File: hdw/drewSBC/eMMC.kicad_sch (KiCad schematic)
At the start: 0 parts

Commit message: added emmc sheet contents
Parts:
- added C? (x4): 0.1uF, Capacitors_SMD:C_0402, symbol Custom_Library:C_Custom
- added C?: 2.2uF, Capacitors_SMD:C_0402, symbol Custom_Library:C_Custom
- added C?: 10uF, Capacitors_SMD:C_1206, symbol Custom_Library:C_Custom
- added R? (x11): 10k, Resistors_SMD:R_0402, symbol Custom_Library:R_Custom
- added U?: EMMC04G-M627-A01, BGA153C50P14X14_1300X1150X100, symbol Custom Library:EMMC04G-M627-A01
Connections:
- new net: C?.1, U?.C2 (VDDI)
- new net +3.3V: C?.1, C?.1, C?.1, C?.1, C?.1, R?.1, R?.1, R?.1, R?.1, R?.1, R?.1, R?.1, R?.1, R?.1, R?.1, R?.1, U?.C6 (VCCQ), U?.E6 (VCC), U?.F5 (VCC), U?.J10 (VCC), U?.K9 (VCC), U?.M4 (VCCQ), U?.N4 (VCCQ), U?.P3 (VCCQ), U?.P5 (VCCQ)
- new net GND: C?.2, C?.2, C?.2, C?.2, C?.2, C?.2, U?.A6 (VSS), U?.C4 (VSSQ), U?.E7 (VSS), U?.G5 (VSS), U?.H10 (VSS), U?.J5 (VSS), U?.K8 (VSS), U?.N2 (VSSQ), U?.N5 (VSSQ), U?.P4 (VSSQ), U?.P6 (VSSQ)
- new net MMC_CLK: R?.2, U?.M6 (CLK)
- new net MMC_CMD: R?.2, U?.M5 (CMD)
- new net MMC_DAT0: R?.2, U?.A3 (DAT0)
- new net MMC_DAT1: R?.2, U?.A4 (DAT1)
- new net MMC_DAT2: R?.2, U?.A5 (DAT2)
- new net MMC_DAT3: R?.2, U?.B2 (DAT3)
- new net MMC_DAT4: R?.2, U?.B3 (DAT4)
- new net MMC_DAT5: R?.2, U?.B4 (DAT5)
- new net MMC_DAT6: R?.2, U?.B5 (DAT6)
- new net MMC_DAT7: R?.2, U?.B6 (DAT7)
- new net ~{MMC_RST}: R?.2, U?.K5 (~{RST})
- no-connect marks 0 -> 1

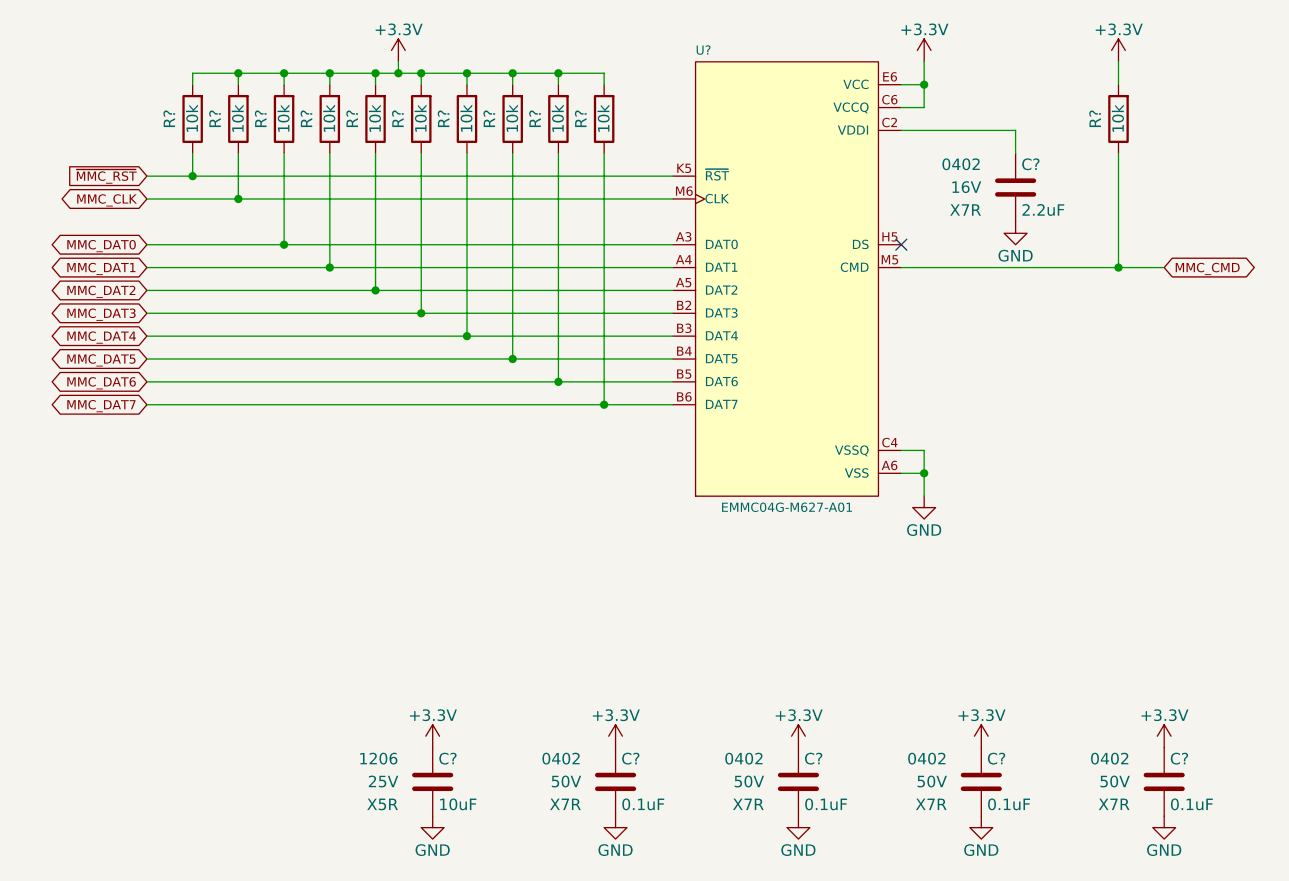
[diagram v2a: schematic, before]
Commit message: ripped up ETH phy
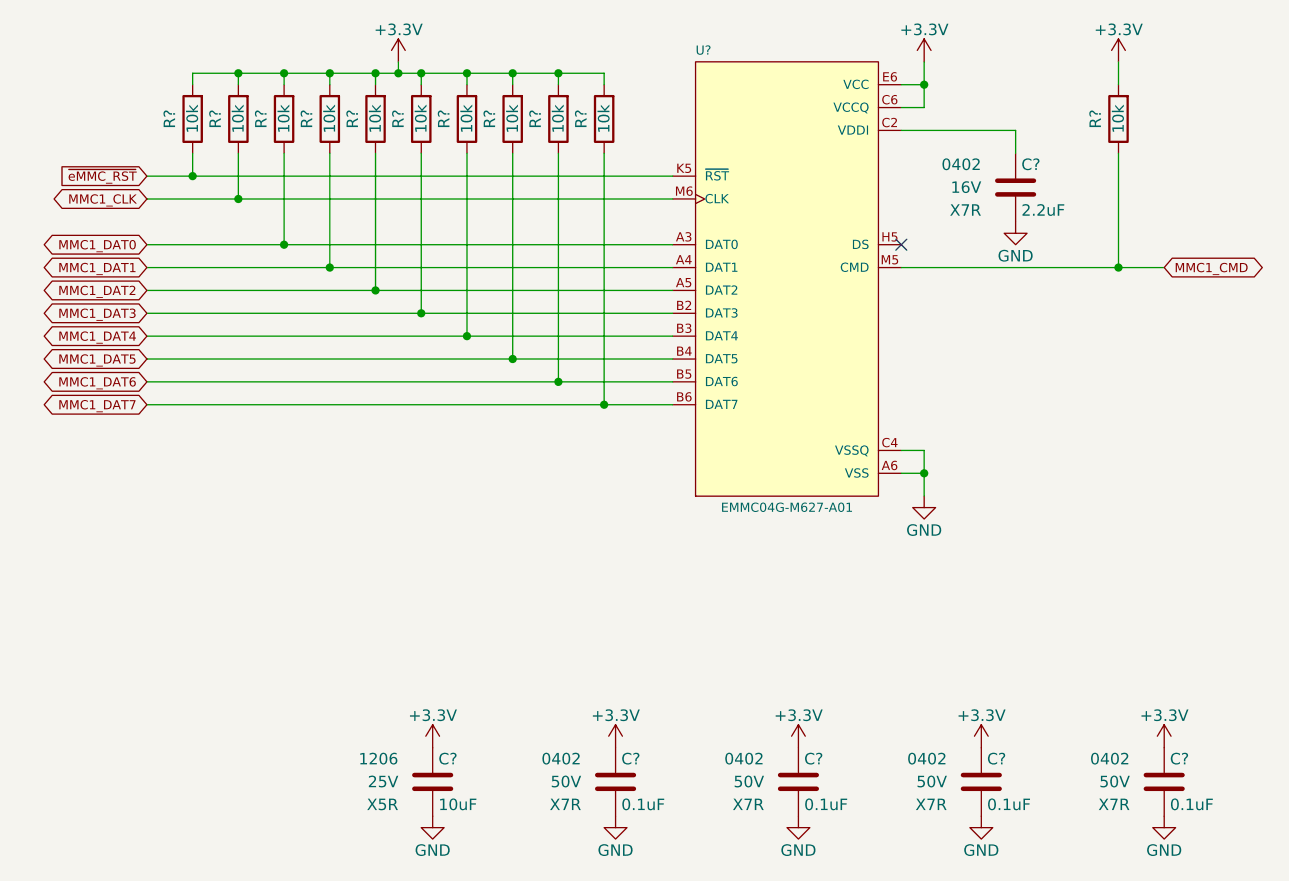
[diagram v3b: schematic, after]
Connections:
- net MMC_CLK renamed MMC1_CLK
- net MMC_CMD renamed MMC1_CMD
- net MMC_DAT0 renamed MMC1_DAT0
- net MMC_DAT1 renamed MMC1_DAT1
- net MMC_DAT2 renamed MMC1_DAT2
- net MMC_DAT3 renamed MMC1_DAT3
- net MMC_DAT4 renamed MMC1_DAT4
- net MMC_DAT5 renamed MMC1_DAT5
- net MMC_DAT6 renamed MMC1_DAT6
- net MMC_DAT7 renamed MMC1_DAT7
- net ~{MMC_RST} renamed ~{eMMC_RST}
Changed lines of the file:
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@@
     (stroke (width 0) (type default) (color 0 0 0 0))
   )
-  (global_label "MMC_DAT0" (shape bidirectional) (at 69.85 83.82 180) (fields_autoplaced)
+  (global_label "MMC1_DAT0" (shape bidirectional) (at 69.85 83.82 180) (fields_autoplaced)
     (effects (font (size 1.016 1.016)) (justify right))
-    (property "Intersheet References" "${INTERSHEET_REFS}" (id 0) (at 60.1786 83.7565 0)
+    (property "Intersheet References" "${INTERSHEET_REFS}" (id 0) (at 59.211 83.7565 0)
       (effects (font (size 1.016 1.016)) (justify right))
     )
   )
-  (global_label "MMC_CMD" (shape bidirectional) (at 182.88 86.36 0) (fields_autoplaced)
+  (global_label "MMC1_CMD" (shape bidirectional) (at 182.88 86.36 0) (fields_autoplaced)
     (effects (font (size 1.016 1.016)) (justify left))
-    (property "Intersheet References" "${INTERSHEET_REFS}" (id 0) (at 192.1159 86.2965 0)
+    (property "Intersheet References" "${INTERSHEET_REFS}" (id 0) (at 193.0835 86.2965 0)
       (effects (font (size 1.016 1.016)) (justify left))
     )
   )
-  (global_label "MMC_DAT6" (shape bidirectional) (at 69.85 99.06 180) (fields_autoplaced)
+  (global_label "MMC1_DAT6" (shape bidirectional) (at 69.85 99.06 180) (fields_autoplaced)
     (effects (font (size 1.016 1.016)) (justify right))
-    (property "Intersheet References" "${INTERSHEET_REFS}" (id 0) (at 60.1786 98.9965 0)
+    (property "Intersheet References" "${INTERSHEET_REFS}" (id 0) (at 59.211 98.9965 0)
       (effects (font (size 1.016 1.016)) (justify right))
     )
   )
-  (global_label "MMC_DAT5" (shape bidirectional) (at 69.85 96.52 180) (fields_autoplaced)
+  (global_label "MMC1_DAT5" (shape bidirectional) (at 69.85 96.52 180) (fields_autoplaced)
     (effects (font (size 1.016 1.016)) (justify right))
-    (property "Intersheet References" "${INTERSHEET_REFS}" (id 0) (at 60.1786 96.4565 0)
+    (property "Intersheet References" "${INTERSHEET_REFS}" (id 0) (at 59.211 96.4565 0)
       (effects (font (size 1.016 1.016)) (justify right))
     )
   )
-  (global_label "MMC_DAT2" (shape bidirectional) (at 69.85 88.9 180) (fields_autoplaced)
+  (global_label "MMC1_DAT2" (shape bidirectional) (at 69.85 88.9 180) (fields_autoplaced)
     (effects (font (size 1.016 1.016)) (justify right))
-    (property "Intersheet References" "${INTERSHEET_REFS}" (id 0) (at 60.1786 88.8365 0)
+    (property "Intersheet References" "${INTERSHEET_REFS}" (id 0) (at 59.211 88.8365 0)
       (effects (font (size 1.016 1.016)) (justify right))
     )
   )
-  (global_label "MMC_DAT4" (shape bidirectional) (at 69.85 93.98 180) (fields_autoplaced)
+  (global_label "MMC1_DAT4" (shape bidirectional) (at 69.85 93.98 180) (fields_autoplaced)
     (effects (font (size 1.016 1.016)) (justify right))
-    (property "Intersheet References" "${INTERSHEET_REFS}" (id 0) (at 60.1786 93.9165 0)
+    (property "Intersheet References" "${INTERSHEET_REFS}" (id 0) (at 59.211 93.9165 0)
       (effects (font (size 1.016 1.016)) (justify right))
     )
   )
-  (global_label "MMC_DAT3" (shape bidirectional) (at 69.85 91.44 180) (fields_autoplaced)
+  (global_label "MMC1_DAT3" (shape bidirectional) (at 69.85 91.44 180) (fields_autoplaced)
     (effects (font (size 1.016 1.016)) (justify right))
-    (property "Intersheet References" "${INTERSHEET_REFS}" (id 0) (at 60.1786 91.3765 0)
+    (property "Intersheet References" "${INTERSHEET_REFS}" (id 0) (at 59.211 91.3765 0)
       (effects (font (size 1.016 1.016)) (justify right))
     )
   )
-  (global_label "MMC_DAT7" (shape bidirectional) (at 69.85 101.6 180) (fields_autoplaced)
+  (global_label "MMC1_DAT7" (shape bidirectional) (at 69.85 101.6 180) (fields_autoplaced)
     (effects (font (size 1.016 1.016)) (justify right))
-    (property "Intersheet References" "${INTERSHEET_REFS}" (id 0) (at 60.1786 101.5365 0)
+    (property "Intersheet References" "${INTERSHEET_REFS}" (id 0) (at 59.211 101.5365 0)
       (effects (font (size 1.016 1.016)) (justify right))
     )
   )
-  (global_label "~{MMC_RST}" (shape input) (at 69.85 76.2 180) (fields_autoplaced)
+  (global_label "~{eMMC_RST}" (shape input) (at 69.85 76.2 180) (fields_autoplaced)
     (effects (font (size 1.016 1.016)) (justify right))
-    (property "Intersheet References" "${INTERSHEET_REFS}" (id 0) (at 61.0495 76.1365 0)
+    (property "Intersheet References" "${INTERSHEET_REFS}" (id 0) (at 60.1786 76.1365 0)
       (effects (font (size 1.016 1.016)) (justify right))
     )
   )
-  (global_label "MMC_DAT1" (shape bidirectional) (at 69.85 86.36 180) (fields_autoplaced)
+  (global_label "MMC1_DAT1" (shape bidirectional) (at 69.85 86.36 180) (fields_autoplaced)
     (effects (font (size 1.016 1.016)) (justify right))
-    (property "Intersheet References" "${INTERSHEET_REFS}" (id 0) (at 60.1786 86.2965 0)
+    (property "Intersheet References" "${INTERSHEET_REFS}" (id 0) (at 59.211 86.2965 0)
       (effects (font (size 1.016 1.016)) (justify right))
     )
   )
-  (global_label "MMC_CLK" (shape bidirectional) (at 69.85 78.74 180) (fields_autoplaced)
+  (global_label "MMC1_CLK" (shape bidirectional) (at 69.85 78.74 180) (fields_autoplaced)
     (effects (font (size 1.016 1.016)) (justify right))
-    (property "Intersheet References" "${INTERSHEET_REFS}" (id 0) (at 60.9527 78.6765 0)
+    (property "Intersheet References" "${INTERSHEET_REFS}" (id 0) (at 59.9851 78.6765 0)
       (effects (font (size 1.016 1.016)) (justify right))
     )
